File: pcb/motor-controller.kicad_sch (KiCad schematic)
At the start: 0 parts

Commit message: [journal] add 6/10 schematic entry
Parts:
- added J1: Conn_01x02_Socket, Connector_JST:JST_PH_B2B-PH-K_1x02_P2.00mm_Vertical, symbol Connector:Conn_01x02_Socket
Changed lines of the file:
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@@
 	(generator_version "9.0")
 	(paper "A4")
+	(symbol
+		(lib_id "Connector:Conn_01x02_Socket")
+		(at 25.4 22.86 180)
+		(unit 1)
+		(exclude_from_sim no)
+		(in_bom yes)
+		(on_board yes)
+		(dnp no)
+		(fields_autoplaced yes)
+		(property "Reference" "J1"
+			(at 26.035 15.24 0)
+			(effects
+				(font
+					(size 1.27 1.27)
+				)
+			)
+		)
+		(property "Value" "Conn_01x02_Socket"
+			(at 26.035 17.78 0)
+			(effects
+				(font
+					(size 1.27 1.27)
+				)
+			)
+		)
+		(property "Footprint" "Connector_JST:JST_PH_B2B-PH-K_1x02_P2.00mm_Vertical"
+			(at 25.4 22.86 0)
+			(effects
+				(font
+					(size 1.27 1.27)
+				)
+				(hide yes)
+			)
+		)
+		(property "Datasheet" "~"
+			(at 25.4 22.86 0)
+			(effects
+				(font
+					(size 1.27 1.27)
+				)
+				(hide yes)
+			)
+		)
+		(property "Description" "Generic connector, single row, 01x02, script generated"
+			(at 25.4 22.86 0)
+			(effects
+				(font
+					(size 1.27 1.27)
+				)
+				(hide yes)
+			)
+		)
+		(pin "2"
+		)
+		(pin "1"
+		)
+		(instances
+			(project ""
+				(path "/c0be3de2-9de4-4447-aa6f-537ea5f31aac/91998897-ec5d-48d5-9630-10203f145e94"
+					(reference "J1")
+					(unit 1)
+				)
+			)
+		)
+	)
 )

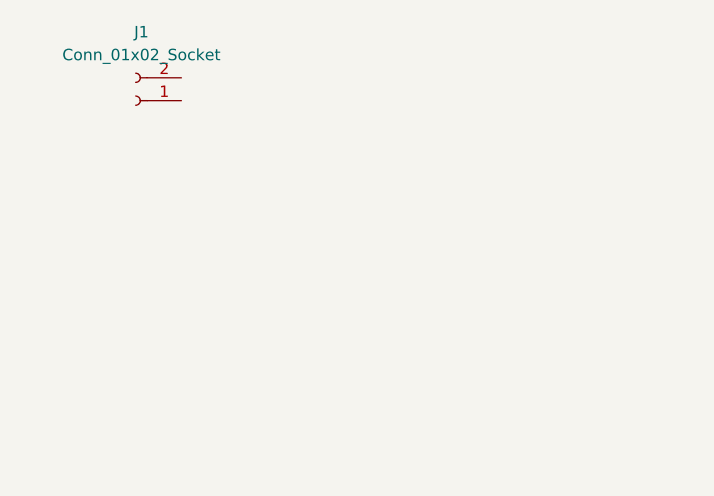
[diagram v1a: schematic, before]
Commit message: [pcb] initial motor controller
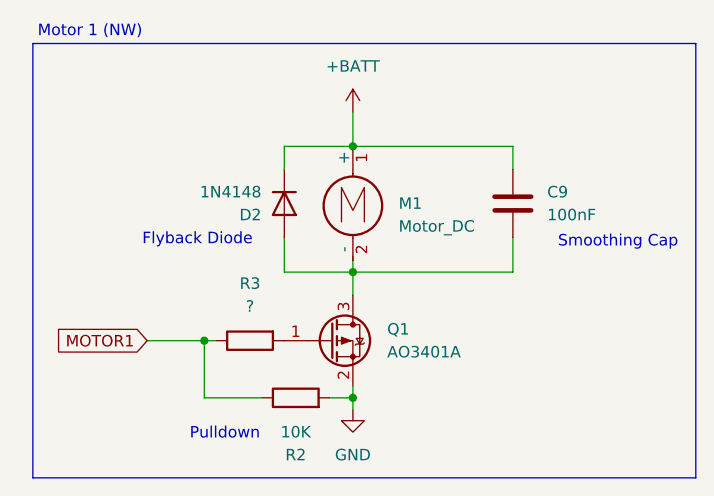
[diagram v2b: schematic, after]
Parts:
- removed J1: Conn_01x02_Socket, Connector_JST:JST_PH_B2B-PH-K_1x02_P2.00mm_Vertical, symbol Connector:Conn_01x02_Socket
- added C9: 100nF, symbol Device:C
- added D2: 1N4148, Diode_THT:D_DO-35_SOD27_P7.62mm_Horizontal, symbol Diode:1N4148
- added M1: Motor_DC, Connector_PinHeader_2.54mm:PinHeader_1x02_P2.54mm_Vertical, symbol Motor:Motor_DC
- added Q1: AO3401A, Package_TO_SOT_SMD:SOT-23, symbol Transistor_FET:AO3401A
- added R2: 10K, symbol Device:R
- added R3: ?, symbol Device:R
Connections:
- new net: C9.2, D2.2 (A), M1.2 (-), Q1.3 (D)
- new net: Q1.1 (G), R3.2
- new net +BATT: C9.1, D2.1 (K), M1.1 (+)
- new net GND: Q1.2 (S), R2.2
- new net MOTOR1: R2.1, R3.1
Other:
- note added: "Flyback Diode"
- note added: "Motor 1 (NW)"
- note added: "Pulldown"
- note added: "Smoothing Cap"

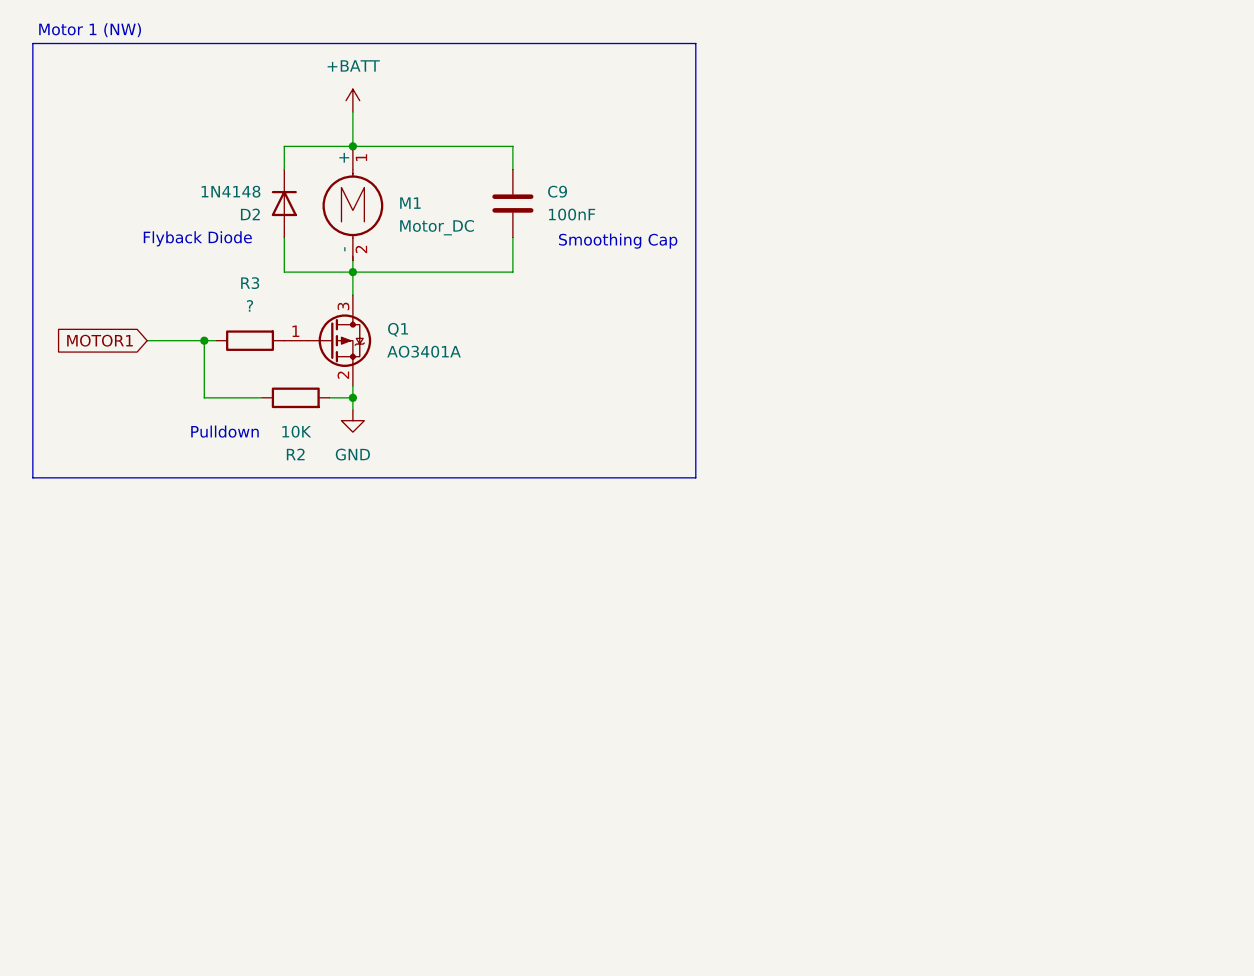
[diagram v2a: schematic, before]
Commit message: [pcb] motor controllers, label/group cleanup
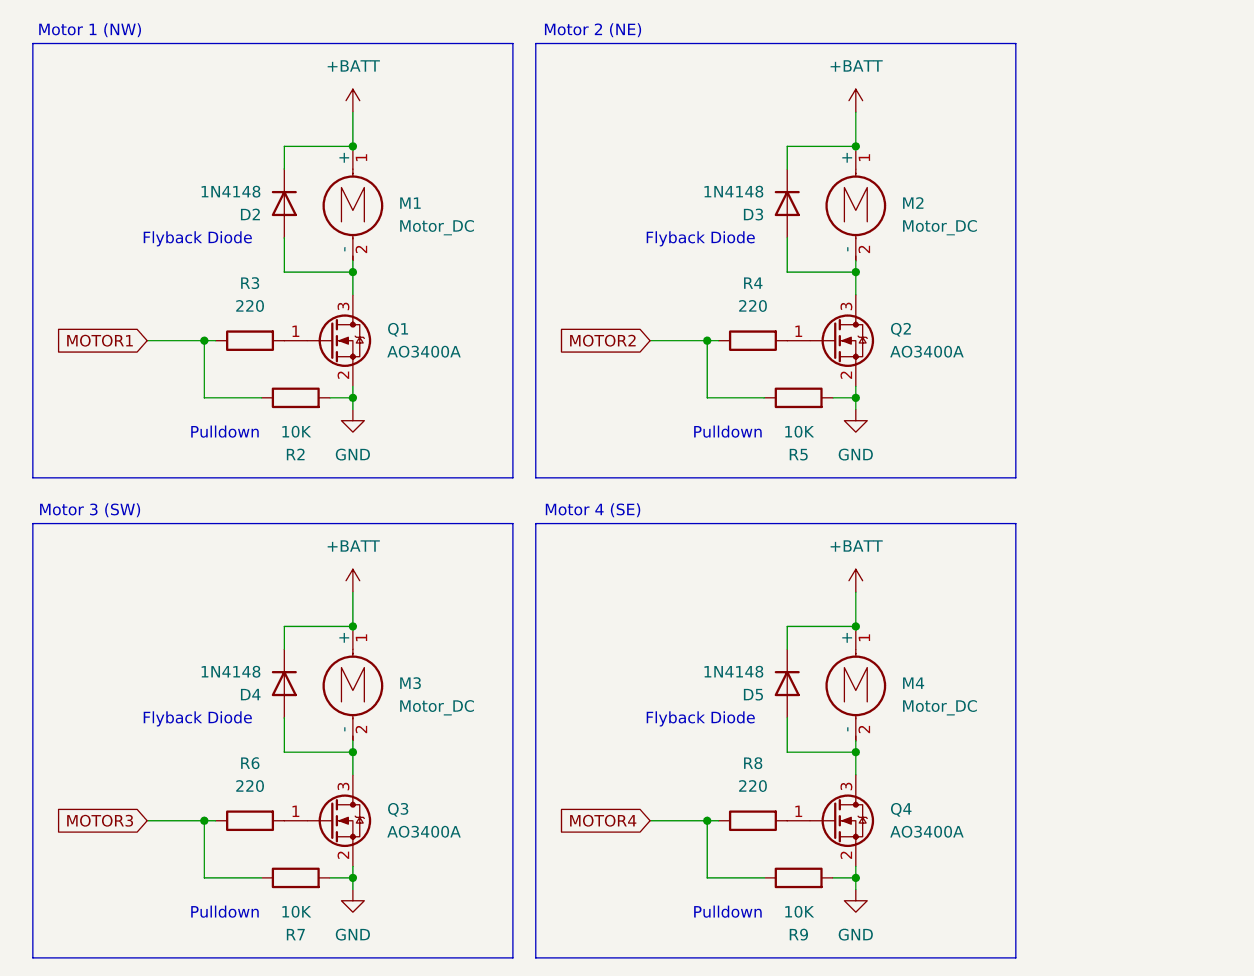
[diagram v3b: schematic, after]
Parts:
- removed C9: 100nF, symbol Device:C
- removed Q1: AO3401A, Package_TO_SOT_SMD:SOT-23, symbol Transistor_FET:AO3401A
- added D3, D4, D5: 1N4148, Diode_THT:D_DO-35_SOD27_P7.62mm_Horizontal, symbol Diode:1N4148
- added M2, M3, M4: Motor_DC, Connector_PinHeader_2.54mm:PinHeader_1x02_P2.54mm_Vertical, symbol Motor:Motor_DC
- added Q1, Q2, Q3, Q4: AO3400A, Package_TO_SOT_SMD:SOT-23, symbol Transistor_FET:AO3400A
- added R4, R6, R8: 220, symbol Device:R
- added R5, R7, R9: 10K, symbol Device:R
- R3: value ? -> 220
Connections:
- net +BATT: now also D3.1 (K), D4.1 (K), D5.1 (K), M2.1 (+), M3.1 (+), M4.1 (+)
- net GND: now also Q1.2 (S), Q2.2 (S), Q3.2 (S), Q4.2 (S), R5.2, R7.2, R9.2
- net at D2.2 (A), M1.2 (-): now also Q1.3 (D)
- net at R3.2: now also Q1.1 (G)
- new net: D5.2 (A), M4.2 (-), Q4.3 (D)
- new net: Q4.1 (G), R8.2
- new net: D3.2 (A), M2.2 (-), Q2.3 (D)
- new net: D4.2 (A), M3.2 (-), Q3.3 (D)
- new net: Q3.1 (G), R6.2
- new net: Q2.1 (G), R4.2
- new net MOTOR2: R4.1, R5.1
- new net MOTOR3: R6.1, R7.1
- new net MOTOR4: R8.1, R9.1
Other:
- note added: "Motor 2 (NE)"
- note added: "Motor 3 (SW)"
- note added: "Motor 4 (SE)"
- note removed: "Smoothing Cap"

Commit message: [pcb] gpio selection, camera, crystal
- Each motors is connected to a channel of TIM1
- The battery voltage divider is connected to ADC1
- The NRF24 is connected to SPI2
- Added OV5640 camera (FPC connector) + LDOs
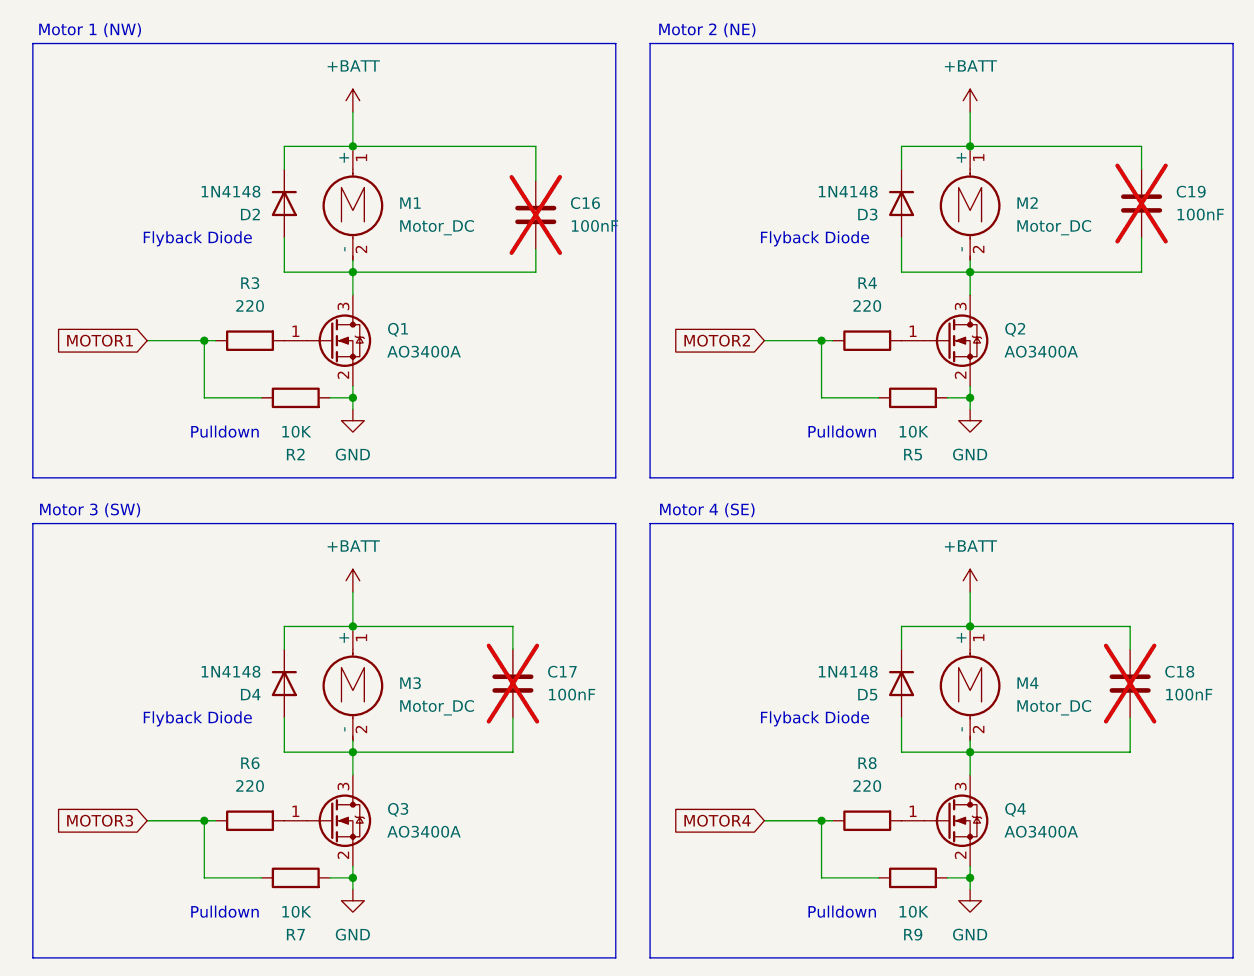
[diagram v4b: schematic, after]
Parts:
- added C16, C17, C18, C19: 100nF, symbol Device:C
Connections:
- net +BATT: now also C16.1, C17.1, C18.1, C19.1
- net at D2.2 (A), M1.2 (-), Q1.3 (D): now also C16.2
- net at D5.2 (A), M4.2 (-), Q4.3 (D): now also C18.2
- net at D3.2 (A), M2.2 (-), Q2.3 (D): now also C19.2
- net at D4.2 (A), M3.2 (-), Q3.3 (D): now also C17.2
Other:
- moved on the sheet: D3, D5, M2, M4, Q2, Q4, R4, R5, R8, R9

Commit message: [bom] pcb components and [pcb] assign footprints
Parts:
- C18: renamed from C19; footprint (none) -> Capacitor_SMD:C_0805_2012Metric_Pad1.18x1.45mm_HandSolder
- C19: renamed from C16; footprint (none) -> Capacitor_SMD:C_0805_2012Metric_Pad1.18x1.45mm_HandSolder
- C20: renamed from C17; footprint (none) -> Capacitor_SMD:C_0805_2012Metric_Pad1.18x1.45mm_HandSolder
- C21: renamed from C18; footprint (none) -> Capacitor_SMD:C_0805_2012Metric_Pad1.18x1.45mm_HandSolder
- D1: renamed from D2; footprint Diode_THT:D_DO-35_SOD27_P7.62mm_Horizontal -> Diode_SMD:D_SOD-323_HandSoldering
- D2: renamed from D3; footprint Diode_THT:D_DO-35_SOD27_P7.62mm_Horizontal -> Diode_SMD:D_SOD-323_HandSoldering
- D3: renamed from D4; footprint Diode_THT:D_DO-35_SOD27_P7.62mm_Horizontal -> Diode_SMD:D_SOD-323_HandSoldering
- D4: renamed from D5; footprint Diode_THT:D_DO-35_SOD27_P7.62mm_Horizontal -> Diode_SMD:D_SOD-323_HandSoldering
- M1, M2, M3, M4: footprint Connector_PinHeader_2.54mm:PinHeader_1x02_P2.54mm_Vertical -> Connector_Wire:SolderWire-0.1sqmm_1x02_P3.6mm_D0.4mm_OD1mm
- Q1, Q2, Q3, Q4: footprint Package_TO_SOT_SMD:SOT-23 -> Package_TO_SOT_SMD:SOT-23_Handsoldering
- R10: renamed from R7; value 10K -> 10k; footprint (none) -> Resistor_SMD:R_0805_2012Metric_Pad1.20x1.40mm_HandSolder
- R11: renamed from R9; value 10K -> 10k; footprint (none) -> Resistor_SMD:R_0805_2012Metric_Pad1.20x1.40mm_HandSolder
- R4: renamed from R3; footprint (none) -> Resistor_SMD:R_0805_2012Metric_Pad1.20x1.40mm_HandSolder
- R5: renamed from R4; footprint (none) -> Resistor_SMD:R_0805_2012Metric_Pad1.20x1.40mm_HandSolder
- R6: renamed from R2; value 10K -> 10k; footprint (none) -> Resistor_SMD:R_0805_2012Metric_Pad1.20x1.40mm_HandSolder
- R7: renamed from R5; value 10K -> 10k; footprint (none) -> Resistor_SMD:R_0805_2012Metric_Pad1.20x1.40mm_HandSolder
- R8: renamed from R6; footprint (none) -> Resistor_SMD:R_0805_2012Metric_Pad1.20x1.40mm_HandSolder
- R9: renamed from R8; footprint (none) -> Resistor_SMD:R_0805_2012Metric_Pad1.20x1.40mm_HandSolder

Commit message: [pcb] add some 3d mooodels
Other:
- note added: "Motor 1 (SE)"
- note added: "Motor 2 (SW)"
- note added: "Motor 3 (NE)"
- note added: "Motor 4 (NW)"
- note removed: "Motor 1 (NW)"
- note removed: "Motor 2 (NE)"
- note removed: "Motor 3 (SW)"
- note removed: "Motor 4 (SE)"
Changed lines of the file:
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@@
 		)
 	)
-	(text "Motor 2 (NE)"
+	(text "Motor 2 (SW)"
 		(exclude_from_sim no)
 		(at 88.9 15.24 0)
@@
 		)
 	)
-	(text "Motor 1 (NW)"
+	(text "Motor 1 (SE)"
 		(exclude_from_sim no)
 		(at 20.32 15.24 0)
@@
 		)
 	)
-	(text "Motor 3 (SW)"
+	(text "Motor 3 (NE)"
 		(exclude_from_sim no)
 		(at 20.32 68.58 0)
@@
 		)
 	)
-	(text "Motor 4 (SE)"
+	(text "Motor 4 (NW)"
 		(exclude_from_sim no)
 		(at 88.9 68.58 0)
